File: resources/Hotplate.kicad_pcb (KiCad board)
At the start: 2 copper layers, 100 x 100 mm, 7 parts, among them J1 Hotplate_Power_Connection, J2 Hotplate_Power_Connection

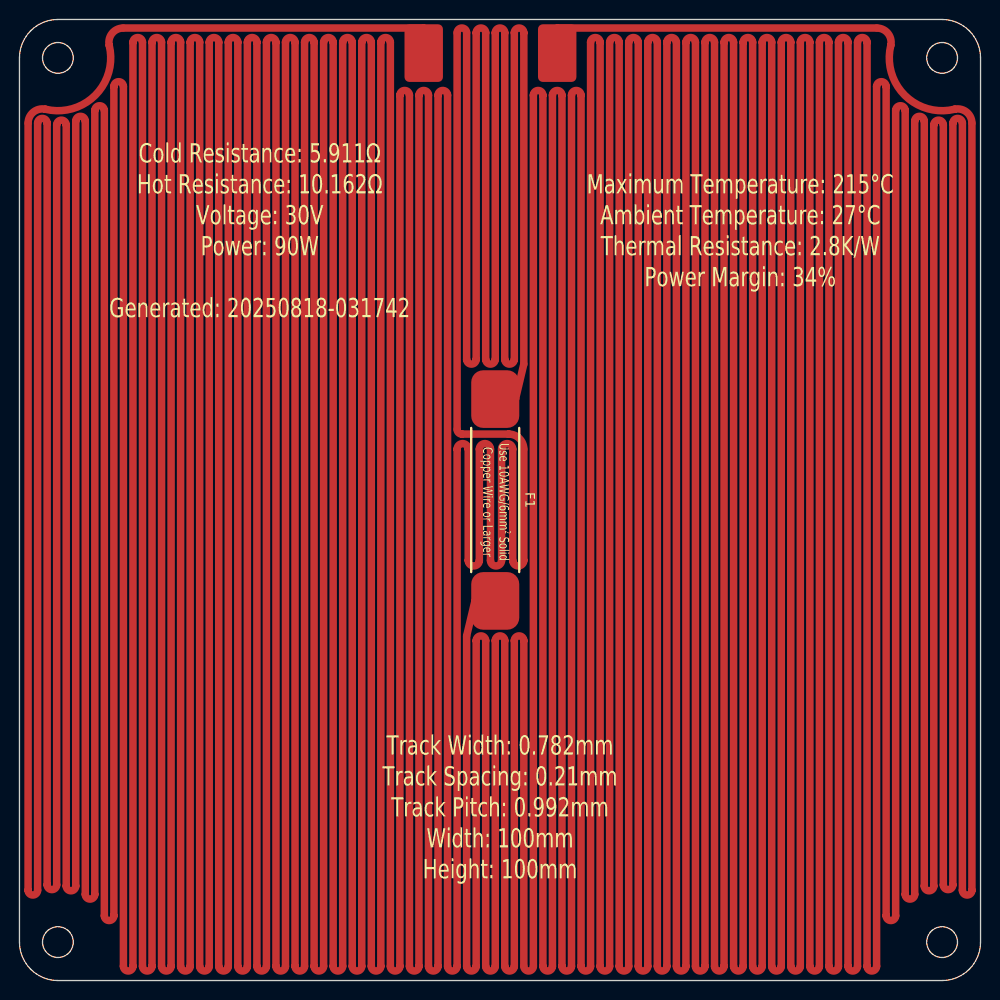
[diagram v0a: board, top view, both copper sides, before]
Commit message: Optimization bug-fixes. UI and analysis enhancements. Refactor optimization into TrackRouter base class.
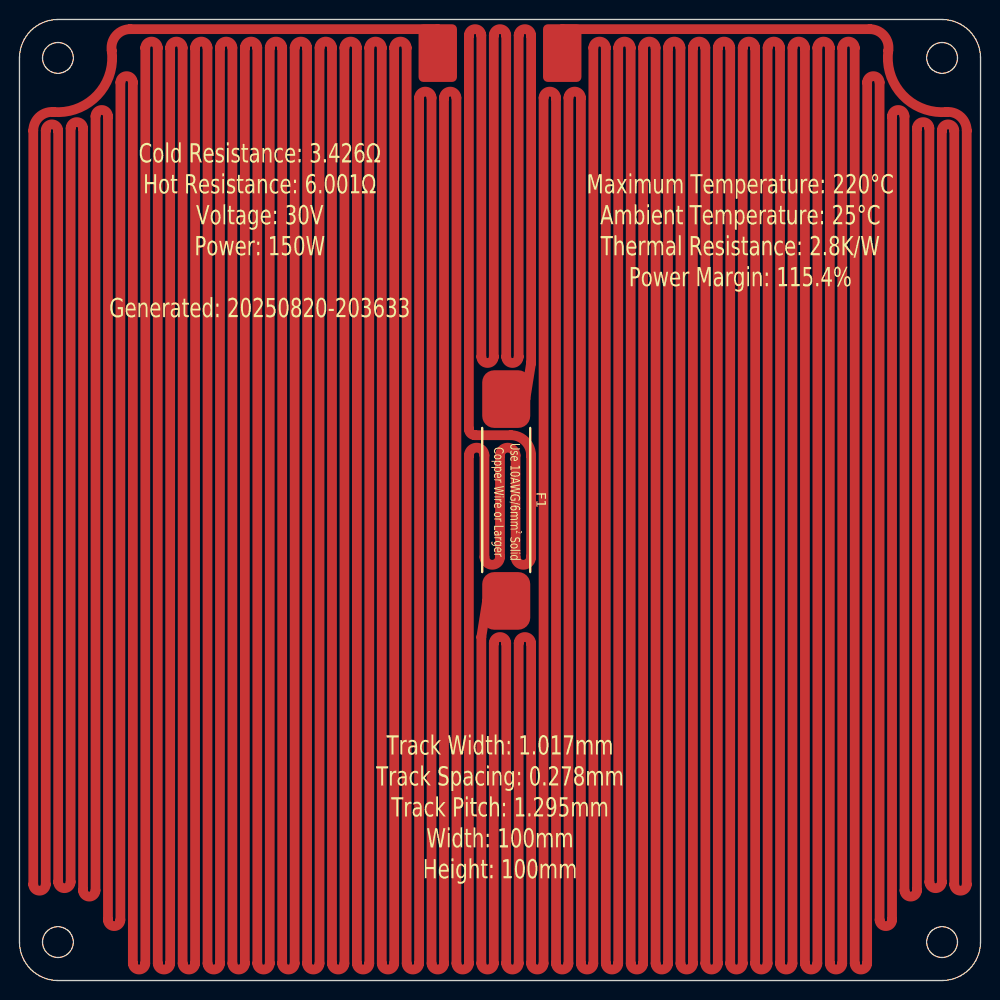
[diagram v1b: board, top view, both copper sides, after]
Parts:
- moved J1 1.46 mm to (98.5, 58.5)
- moved F1 1.14 mm to (105.6, 105.0)
- moved J2 0.52 mm to (111.5, 58.5)
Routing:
- net Net-(J2-Pin_1): track 4697.5 -> 3486.5 mm
- net Net-(J1-Pin_1): track 4684.9 -> 3642.2 mm
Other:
- board text added: "Cold Resistance: 3.426Ω Hot Resistance: 6.001Ω Voltage: 30V Power: 150W Generated: 20250820-203633"
- board text added: "Maximum Temperature: 220°C Ambient Temperature: 25°C Thermal Resistance: 2.8K/W Power Margin: 115.4%"
- board text added: "Track Width: 1.017mm Track Spacing: 0.278mm Track Pitch: 1.295mm Width: 100mm Height: 100mm"
- board text removed: "Cold Resistance: 5.911Ω Hot Resistance: 10.162Ω Voltage: 30V Power: 90W Generated: 20250818-031742"
- board text removed: "Maximum Temperature: 215°C Ambient Temperature: 27°C Thermal Resistance: 2.8K/W Power Margin: 34%"
- board text removed: "Track Width: 0.782mm Track Spacing: 0.21mm Track Pitch: 0.992mm Width: 100mm Height: 100mm"

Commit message: Updates based on test results from first Al PCB samples from JLCPCB.
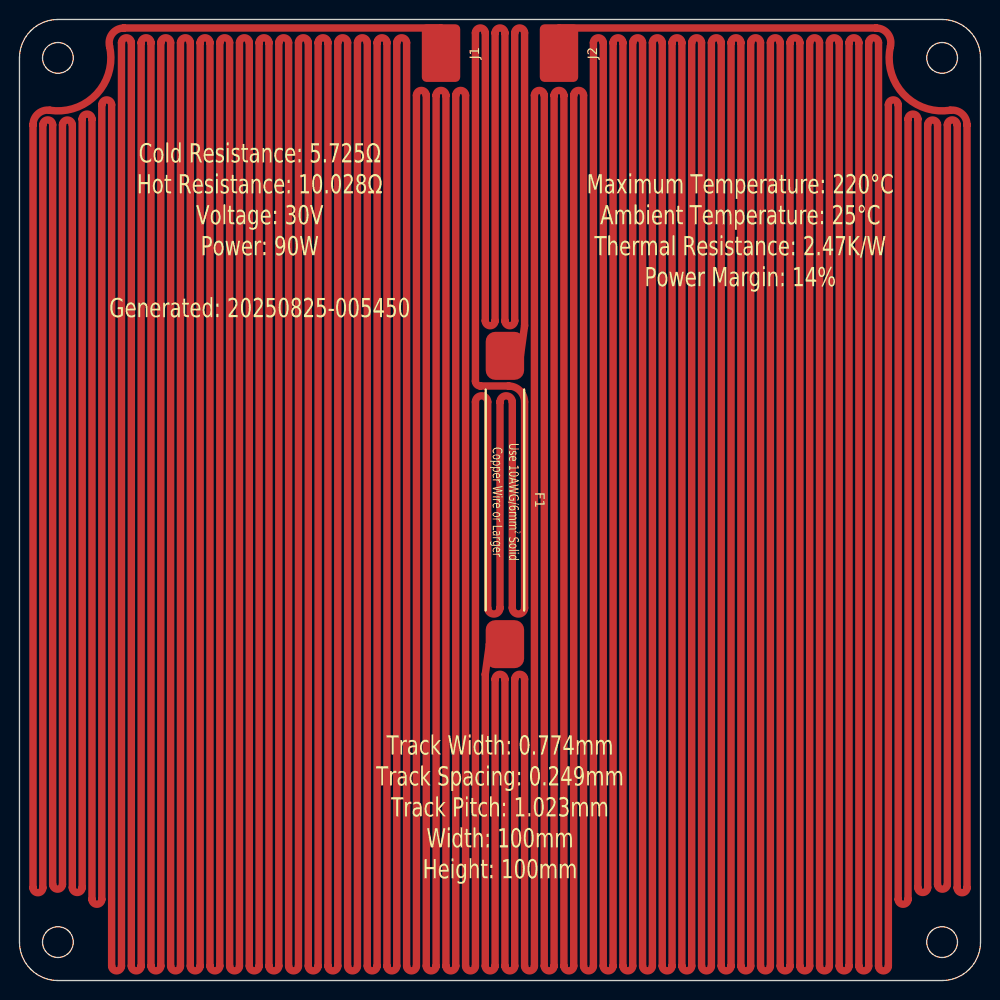
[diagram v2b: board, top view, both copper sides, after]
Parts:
- F1: footprint blg:Thermal Fuse, Front, 25mm -> Hotplate:Thermal Fuse, SN100C, Front, 35mm
- J1, J2: footprint blg:SMD_PowerConnection_4x6mm -> Hotplate:SMD_PowerConnection_4x6mm
- moved J1 0.34 mm to (98.9, 58.5)
- moved J2 0.34 mm to (111.1, 58.5)
- moved F1 0.14 mm to (105.5, 105.0)
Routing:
- net Net-(J1-Pin_1): track 3642.2 -> 4627.3 mm
- net Net-(J2-Pin_1): track 3486.5 -> 4431.1 mm
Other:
- board text added: "Cold Resistance: 5.725Ω Hot Resistance: 10.028Ω Voltage: 30V Power: 90W Generated: 20250825-005450"
- board text added: "Maximum Temperature: 220°C Ambient Temperature: 25°C Thermal Resistance: 2.47K/W Power Margin: 14%"
- board text added: "Track Width: 0.774mm Track Spacing: 0.249mm Track Pitch: 1.023mm Width: 100mm Height: 100mm"
- board text removed: "Cold Resistance: 3.426Ω Hot Resistance: 6.001Ω Voltage: 30V Power: 150W Generated: 20250820-203633"
- board text removed: "Maximum Temperature: 220°C Ambient Temperature: 25°C Thermal Resistance: 2.8K/W Power Margin: 115.4%"
- board text removed: "Track Width: 1.017mm Track Spacing: 0.278mm Track Pitch: 1.295mm Width: 100mm Height: 100mm"
